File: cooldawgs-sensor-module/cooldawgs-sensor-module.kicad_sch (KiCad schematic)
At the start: 4 parts, among them U1 XIAO-nRF52840-DIP, U2 MLX90614ESF-AAA-000-TU

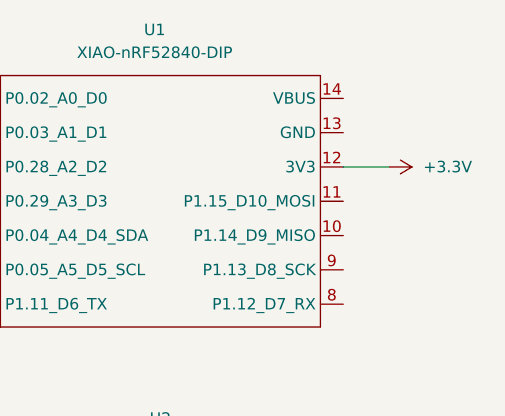
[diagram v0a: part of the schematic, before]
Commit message: added symbols and footprints
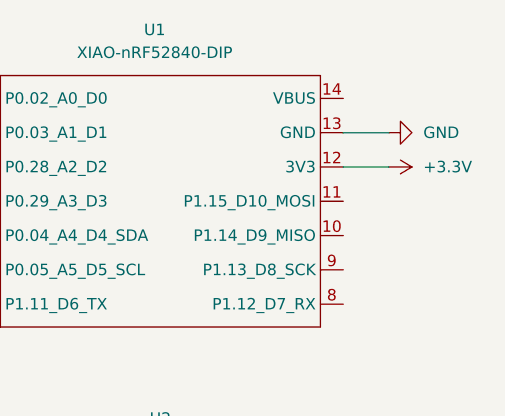
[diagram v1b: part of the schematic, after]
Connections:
- net GND: now also U1.13 (GND)
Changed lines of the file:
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@@
+	(wire
+		(pts
+			(xy 170.18 80.01) (xy 175.26 80.01)
+		)
+		(stroke
+			(width 0)
+			(type default)
+		)
+	)
 	(wire
 		(pts
@@
 					(unit 1)
 				)
+			)
+		)
+	)
+	(symbol
+		(lib_id "power:GND")
+		(at 175.26 80.01 90)
+		(unit 1)
+		(exclude_from_sim no)
+		(in_bom yes)
+		(on_board yes)
+		(dnp no)
+		(fields_autoplaced yes)
+		(property "Reference" "#PWR05"
+			(at 181.61 80.01 0)
+			(effects
+				(font
+					(size 1.27 1.27)
+				)
+				(hide yes)
+			)
+		)
+		(property "Value" "GND"
+			(at 179.07 80.0099 90)
+			(effects
+				(font
+					(size 1.27 1.27)
+				)
+				(justify right)
+			)
+		)
+		(property "Footprint" ""
+			(at 175.26 80.01 0)
+			(effects
+				(font
+					(size 1.27 1.27)
+				)
+				(hide yes)
+			)
+		)
+		(property "Datasheet" ""
+			(at 175.26 80.01 0)
+			(effects
+				(font
+					(size 1.27 1.27)
+				)
+				(hide yes)
+			)
+		)
+		(property "Description" "Power symbol creates a global label with name \"GND\" , ground"
+			(at 175.26 80.01 0)
+			(effects
+				(font
+					(size 1.27 1.27)
+				)
+				(hide yes)
+			)
+		)
+		(pin "1"
+		)
+		(instances
+			(project "cooldawgs-sensor-module"
+				(path "/3eeec553-5bc7-40ba-aaf7-7113d1b1d799"
+					(reference "#PWR05")
+					(unit 1)
+				)

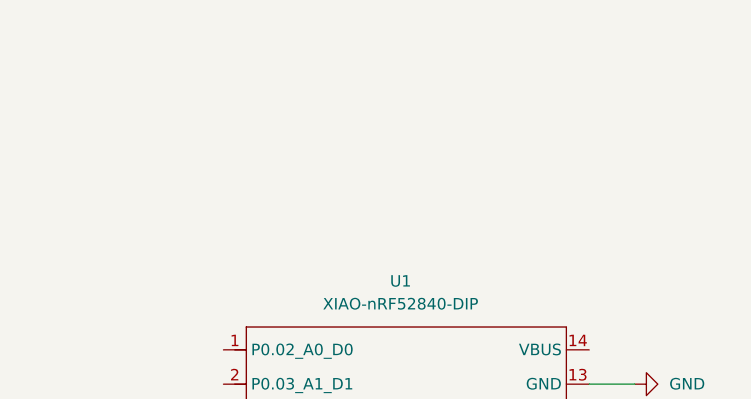
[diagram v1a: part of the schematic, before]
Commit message: added dht22
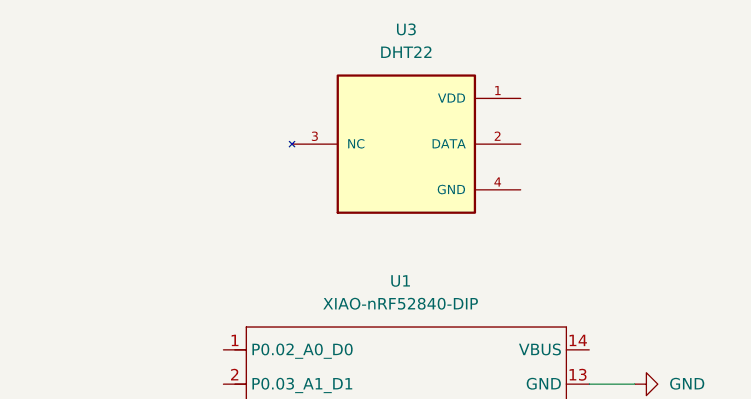
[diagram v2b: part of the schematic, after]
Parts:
- added U3: DHT22, DHT22:XDCR_DHT22, symbol DHT22:DHT22
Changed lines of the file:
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@@
+	)
+	(symbol
+		(lib_id "DHT22:DHT22")
+		(at 149.86 53.34 0)
+		(unit 1)
+		(exclude_from_sim no)
+		(in_bom yes)
+		(on_board yes)
+		(dnp no)
+		(fields_autoplaced yes)
+		(property "Reference" "U3"
+			(at 149.86 40.64 0)
+			(effects
+				(font
+					(size 1.27 1.27)
+				)
+			)
+		)
+		(property "Value" "DHT22"
+			(at 149.86 43.18 0)
+			(effects
+				(font
+					(size 1.27 1.27)
+				)
+			)
+		)
+		(property "Footprint" "DHT22:XDCR_DHT22"
+			(at 149.86 53.34 0)
+			(effects
+				(font
+					(size 1.27 1.27)
+				)
+				(justify bottom)
+				(hide yes)
+			)
+		)
+		(property "Datasheet" ""
+			(at 149.86 53.34 0)
+			(effects
+				(font
+					(size 1.27 1.27)
+				)
+				(hide yes)
+			)
+		)
+		(property "Description" ""
+			(at 149.86 53.34 0)
+			(effects
+				(font
+					(size 1.27 1.27)
+				)
+				(hide yes)
+			)
+		)
+		(property "MF" "Aosong Electronics"
+			(at 149.86 53.34 0)
+			(effects
+				(font
+					(size 1.27 1.27)
+				)
+				(justify bottom)
+				(hide yes)
+			)
+		)
+		(property "MAXIMUM_PACKAGE_HEIGHT" "7.8 mm"
+			(at 149.86 53.34 0)
+			(effects
+				(font
+					(size 1.27 1.27)
+				)
+				(justify bottom)
+				(hide yes)
+			)
+		)
+		(property "CREATOR" "KARTHIK"
+			(at 149.86 53.34 0)
+			(effects
+				(font
+					(size 1.27 1.27)
+				)
+				(justify bottom)
+				(hide yes)
+			)
+		)
+		(property "Price" "None"
+			(at 149.86 53.34 0)
+			(effects
+				(font
+					(size 1.27 1.27)
+				)
+				(justify bottom)
+				(hide yes)
+			)
+		)
+		(property "Package" "Package"
+			(at 149.86 53.34 0)
+			(effects
+				(font
+					(size 1.27 1.27)
+				)
+				(justify bottom)
+				(hide yes)
+			)
+		)
+		(property "Check_prices" "https://www.snapeda.com/parts/DHT22/Aosong+Electronics/view-part/?ref=eda"
+			(at 149.86 53.34 0)
+			(effects
+				(font
+					(size 1.27 1.27)
+				)
+				(justify bottom)
+				(hide yes)
+			)
+		)
+		(property "STANDARD" "IPC-7351B"
+			(at 149.86 53.34 0)
+			(effects
+				(font
+					(size 1.27 1.27)
+				)
+				(justify bottom)
+				(hide yes)
+			)
+		)
+		(property "SnapEDA_Link" "https://www.snapeda.com/parts/DHT22/Aosong+Electronics/view-part/?ref=snap"
+			(at 149.86 53.34 0)
+			(effects
+				(font
+					(size 1.27 1.27)
+				)
+				(justify bottom)
+				(hide yes)
+			)
+		)
+		(property "MP" "DHT22"
+			(at 149.86 53.34 0)
+			(effects
+				(font
+					(size 1.27 1.27)
+				)
+				(justify bottom)
+				(hide yes)
+			)
+		)
+		(property "Description_1" "Capacitive-type humidity and temperature module/sensor"
+			(at 149.86 53.34 0)
+			(effects
+				(font
+					(size 1.27 1.27)
+				)
+				(justify bottom)
+				(hide yes)
+			)
+		)
+		(property "Availability" "Not in stock"
+			(at 149.86 53.34 0)
+			(effects
+				(font
+					(size 1.27 1.27)
+				)
+				(justify bottom)
+				(hide yes)
+			)
+		)
+		(property "MANUFACTURER" "Aosong Electronics"
+			(at 149.86 53.34 0)
+			(effects
+				(font
+					(size 1.27 1.27)
+				)
+				(justify bottom)
+				(hide yes)
+			)
+		)
+		(pin "2"
+		)
+		(pin "1"
+		)
+		(pin "3"
+		)
+		(pin "4"
+		)
+		(instances
+			(project ""
+				(path "/3eeec553-5bc7-40ba-aaf7-7113d1b1d799"
+					(reference "U3")
+					(unit 1)
+				)
+			)
+		)
 	)
 	(symbol
